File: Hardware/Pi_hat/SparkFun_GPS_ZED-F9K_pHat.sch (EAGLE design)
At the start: 41 parts, among them J2 RASPBERRYPI-40-PIN-GPIO_PTH_N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, J4 U.FL, U1 UBLOX_ZED_F9K, U3 TRIPLE_BUFFER_74LVC3G07

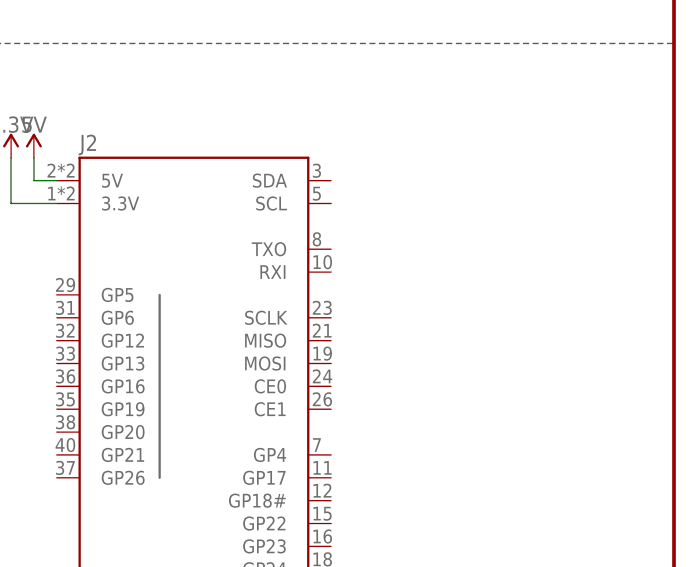
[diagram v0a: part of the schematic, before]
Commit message: Adds nets for data lines
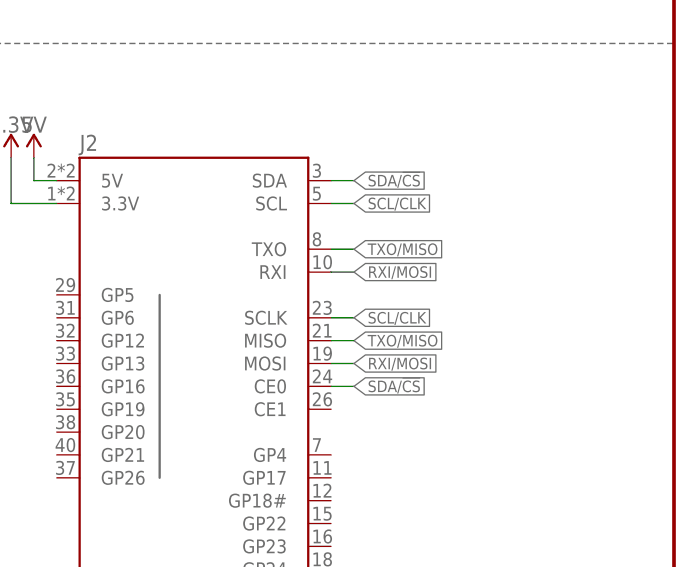
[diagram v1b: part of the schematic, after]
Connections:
- net RXI/MOSI: now also J2.MOSI, J2.RXI
- net SCL/CLK: now also J2.SCL, J2.SCLK
- net SDA/!CS: now also J2.CE0, J2.SDA
- net TXO/MISO: now also J2.MISO, J2.TXO
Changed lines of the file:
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@@
 <label x="99.06" y="231.14" size="1.27" layer="95" font="vector" xref="yes"/>
+</segment>
+<segment>
+<pinref part="J2" gate="G$1" pin="SCL"/>
+<wire x1="393.7" y1="116.84" x2="396.24" y2="116.84" width="0.1524" layer="91"/>
+<label x="396.24" y="116.84" size="1.27" layer="95" font="vector" xref="yes"/>
+</segment>
+<segment>
+<pinref part="J2" gate="G$1" pin="SCLK"/>
+<wire x1="393.7" y1="104.14" x2="396.24" y2="104.14" width="0.1524" layer="91"/>
+<label x="396.24" y="104.14" size="1.27" layer="95" font="vector" xref="yes"/>
 </segment>
 </net>
@@
 <label x="99.06" y="223.52" size="1.27" layer="95" font="vector" xref="yes"/>
 </segment>
+<segment>
+<pinref part="J2" gate="G$1" pin="TXO"/>
+<wire x1="393.7" y1="111.76" x2="396.24" y2="111.76" width="0.1524" layer="91"/>
+<label x="396.24" y="111.76" size="1.27" layer="95" font="vector" xref="yes"/>
+</segment>
+<segment>
+<pinref part="J2" gate="G$1" pin="MISO"/>
+<wire x1="393.7" y1="101.6" x2="396.24" y2="101.6" width="0.1524" layer="91"/>
+<label x="396.24" y="101.6" size="1.27" layer="95" font="vector" xref="yes"/>
+</segment>
 </net>
 <net name="D_SEL" class="0">
@@
 <wire x1="96.52" y1="220.98" x2="99.06" y2="220.98" width="0.1524" layer="91"/>
 <label x="99.06" y="220.98" size="1.27" layer="95" font="vector" xref="yes"/>
+</segment>
+<segment>
+<pinref part="J2" gate="G$1" pin="RXI"/>
+<wire x1="393.7" y1="109.22" x2="396.24" y2="109.22" width="0.1524" layer="91"/>
+<label x="396.24" y="109.22" size="1.27" layer="95" font="vector" xref="yes"/>
+</segment>
+<segment>
+<pinref part="J2" gate="G$1" pin="MOSI"/>
+<wire x1="393.7" y1="99.06" x2="396.24" y2="99.06" width="0.1524" layer="91"/>
+<label x="396.24" y="99.06" size="1.27" layer="95" font="vector" xref="yes"/>
 </segment>
 </net>
@@
 <wire x1="213.36" y1="83.82" x2="193.04" y2="83.82" width="0.1524" layer="91"/>
 </segment>
-</net>
+<segment>
+<pinref part="J2" gate="G$1" pin="SDA"/>
+<wire x1="393.7" y1="119.38" x2="396.24" y2="119.38" width="0.1524" layer="91"/>
+<label x="396.24" y="119.38" size="1.27" layer="95" font="vector" xref="yes"/>
+</segment>
+<segment>
+<pinref part="J2" gate="G$1" pin="CE0"/>
+<wire x1="393.7" y1="96.52" x2="396.24" y2="96.52" width="0.1524" layer="91"/>
+<label x="396.24" y="96.52" size="1.27" layer="95" font="vector" xref="yes"/>
+</segment>
+</net>

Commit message: Finishes pi hat design and adds some labels
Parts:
- added J1: QWIIC_RIGHT_ANGLE, SparkFun-Connectors:QWIIC_CONNECTORJS-1MM
- added J3: (no value), SparkFun-Connectors:CONN_05NO_SILK
- added LOGO1: SFE_LOGO_NAME_FLAME.2_INCH, SparkFun-Aesthetics:SFE_LOGO_NAME_FLAME.2_INCH
- added LOGO2: OSHW-LOGOM, SparkFun-Aesthetics:OSHW-LOGOM
- added LOGO3: QWIIC_LOGO_5MM, SparkFun-Aesthetics:QWIIC_LOGO_5MM
- J5: device SparkFun-Connectors:CONN_05NO_SILK -> SparkFun-Connectors:CONN_06NO_SILK_NO_POP
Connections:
- removed net 5V: J2.5V
- removed net VIN: D4.6
- removed net V_USB: D4.1, J8.VBUS
- new net QWIIC_SCL: J1.4, J2.SCL, R4.1
- new net QWIIC_SDA: J1.3, J2.SDA, R3.1
- net !RESET_OUT: now also J3.4; no longer J5.4
- net !SAFEBOOT_IN: now also J3.3; no longer J5.3
- net 3.3V: now also J1.2
- net GND: now also J1.1, J5.1
- net INT_OUT: now also J3.2; no longer J5.2
- net PPS: now also J3.5; no longer J5.5
- net RXI2: now also J5.4
- net SCL/CLK: no longer J2.SCL, R4.1
- net SDA/!CS: no longer J2.SDA, R3.1
- net TXO2: now also J5.5
- net TX_READY: now also J3.1; no longer J5.1
